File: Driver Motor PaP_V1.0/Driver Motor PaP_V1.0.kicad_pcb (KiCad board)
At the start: 4 copper layers, 60 x 50 mm, 33 parts, among them J1 Conn_01x02, J2 Conn_01x02, J3 Conn_01x03, J4 Conn_01x05, J5 Conn_01x01, J6 Conn_01x02, J7 Conn_01x02, U1 LM358, U2 LM358, U3 LM358

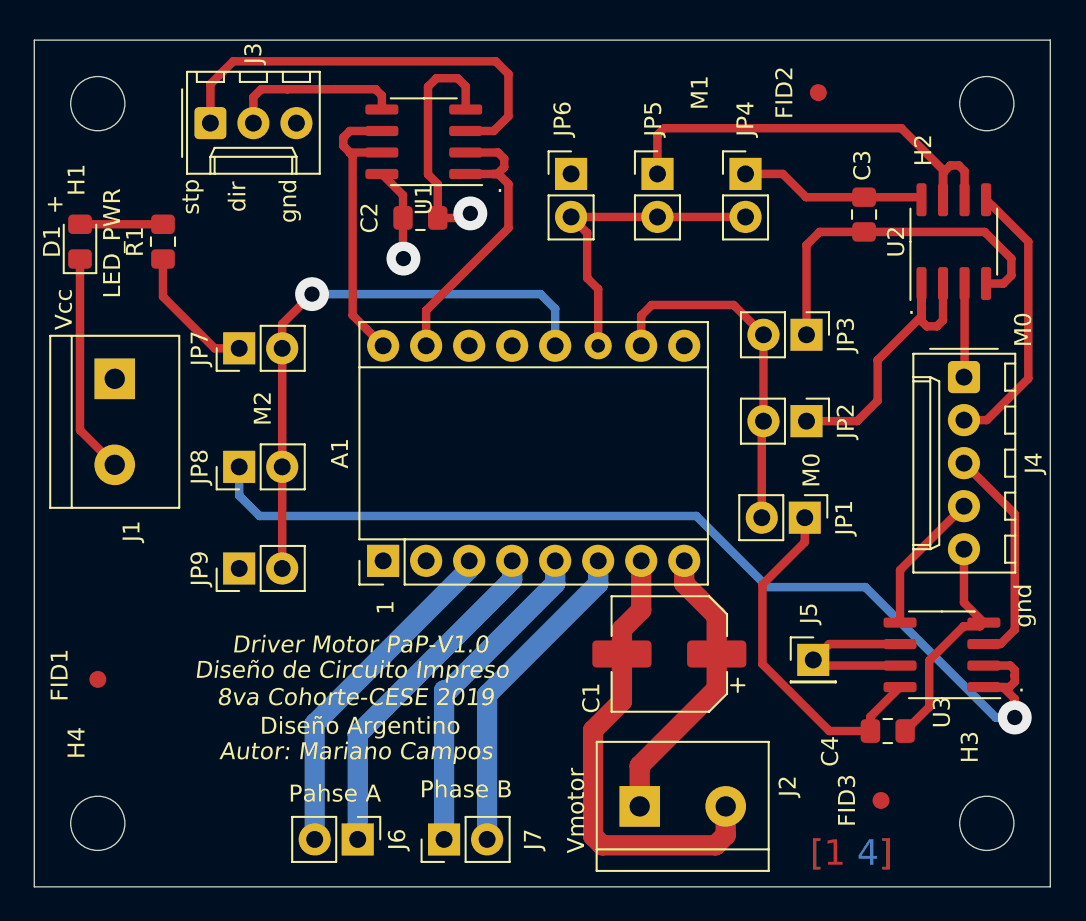
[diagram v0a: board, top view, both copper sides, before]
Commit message: correción dehuellas delos terminales block y modelo 3D
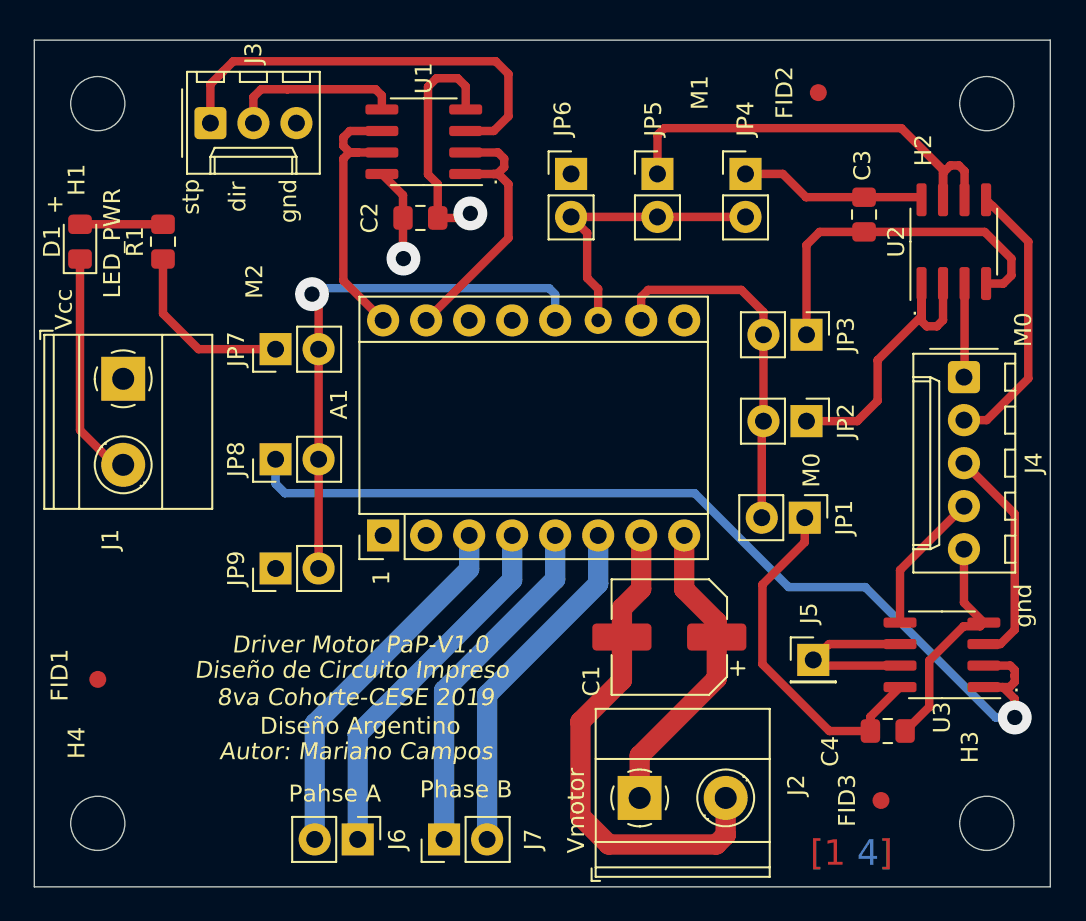
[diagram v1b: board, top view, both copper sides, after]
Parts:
- J1, J2: footprint TerminalBlock:TerminalBlock_bornier-2_P5.08mm -> TerminalBlock_Phoenix:TerminalBlock_Phoenix_MKDS-1,5-2-5.08_1x02_P5.08mm_Horizontal
- moved JP8 2.20 mm to (121.8, 109.8)
- moved JP7 2.15 mm to (121.8, 103.2)
- moved JP9 2.15 mm to (121.8, 116.2)
- moved A1 1.50 mm to (128.1, 114.2)
- moved C1 1.00 mm to (145.0, 120.2)
- moved J1 0.50 mm to (112.8, 105.0)
- moved J2 0.50 mm to (143.2, 129.8)
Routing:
- net VCC: track 45.6 -> 48.1 mm
- net Net-(JP8-Pad1): track 60.8 -> 58.7 mm
- net GNDPWR: track 27.4 -> 29.3 mm
- net Net-(A1-Pad6): track 19.2 -> 20.7 mm
- net Net-(A1-Pad4): track 20.2 -> 21.7 mm
- net Net-(A1-Pad3): track 20.2 -> 21.7 mm
- net Net-(A1-Pad15): track 18.1 -> 16.6 mm
- net Net-(A1-Pad11): track 18.6 -> 17.1 mm
- net Net-(A1-Pad5): track 19.3 -> 20.7 mm
- net Net-(A1-Pad12): track 33.8 -> 32.6 mm
- net VPP: track 17.2 -> 18.2 mm
- net Net-(A1-Pad16): track 17.6 -> 16.9 mm
- net Net-(A1-Pad10): track 20.8 -> 21.5 mm

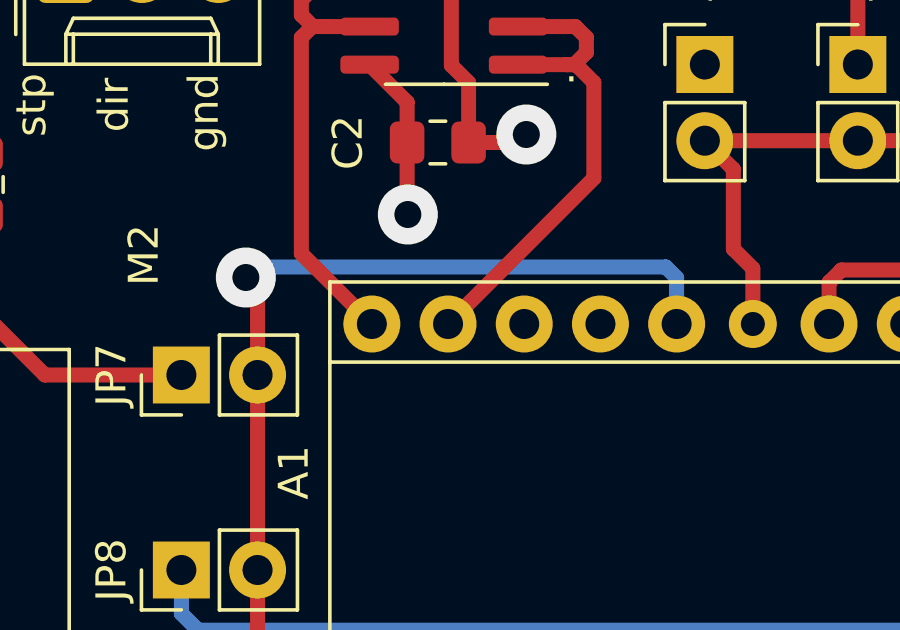
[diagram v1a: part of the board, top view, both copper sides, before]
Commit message: modificación en el ruteo
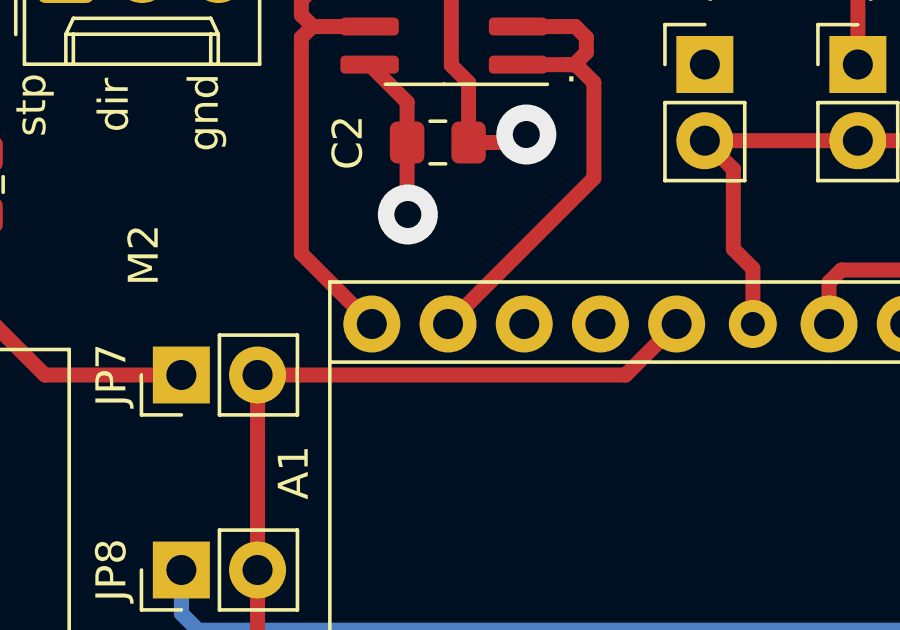
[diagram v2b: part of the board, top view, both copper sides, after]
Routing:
- net Net-(A1-Pad12): track 32.6 -> 27.6 mm, vias 1 -> 0
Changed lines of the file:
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@@
     (thickness 1.6)
     (drawings 39)
-    (tracks 199)
+    (tracks 193)
     (zones 0)
     (modules 33)
@@
     (47 F.CrtYd user)
     (48 B.Fab user)
-    (49 F.Fab user)
+    (49 F.Fab user hide)
   )
   (setup
-    (last_trace_width 1.2)
+    (last_trace_width 0.5)
     (user_trace_width 0.8)
     (user_trace_width 1)
@@
   (segment (start 135.72 116.88) (end 135.72 114.25) (width 1.2) (layer 4-B.Cu) (net 6))
   (segment (start 126.6 126) (end 135.72 116.88) (width 1.2) (layer 4-B.Cu) (net 6))
-  (segment (start 123.9 100) (end 123.9 100) (width 0.5) (layer 1-F.Cu) (net 7))
-  (via (at 123.9 100) (size 2) (drill 0.9) (layers 1-F.Cu 4-B.Cu) (net 7))
   (segment (start 124.29 103.25) (end 124.29 109.75) (width 0.5) (layer 1-F.Cu) (net 7))
   (segment (start 124.29 114.856498) (end 124.29 109.75) (width 0.5) (layer 1-F.Cu) (net 7))
   (segment (start 124.29 116.2) (end 124.29 114.856498) (width 0.5) (layer 1-F.Cu) (net 7))
-  (segment (start 124.29 100.39) (end 123.9 100) (width 0.5) (layer 1-F.Cu) (net 7))
-  (segment (start 124.29 103.25) (end 124.29 100.39) (width 0.5) (layer 1-F.Cu) (net 7))
-  (segment (start 124.249999 99.650001) (end 137.900001 99.650001) (width 0.5) (layer 4-B.Cu) (net 7))
-  (segment (start 123.9 100) (end 124.249999 99.650001) (width 0.5) (layer 4-B.Cu) (net 7))
-  (segment (start 138.26 100.01) (end 138.26 101.55) (width 0.5) (layer 4-B.Cu) (net 7))
-  (segment (start 137.900001 99.650001) (end 138.26 100.01) (width 0.5) (layer 4-B.Cu) (net 7))
+  (segment (start 136.56 103.25) (end 138.26 101.55) (width 0.5) (layer 1-F.Cu) (net 7))
+  (segment (start 124.29 103.25) (end 136.56 103.25) (width 0.5) (layer 1-F.Cu) (net 7))
   (segment (start 131.7 132.2) (end 131.7 123.4) (width 1.2) (layer 4-B.Cu) (net 8))
   (segment (start 138.26 116.84) (end 138.26 114.25) (width 1.2) (layer 4-B.Cu) (net 8))
